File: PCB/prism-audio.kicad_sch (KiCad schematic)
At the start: 8 parts, among them Q1 PMBT3904_215, U1 ADAU1761BCPZ

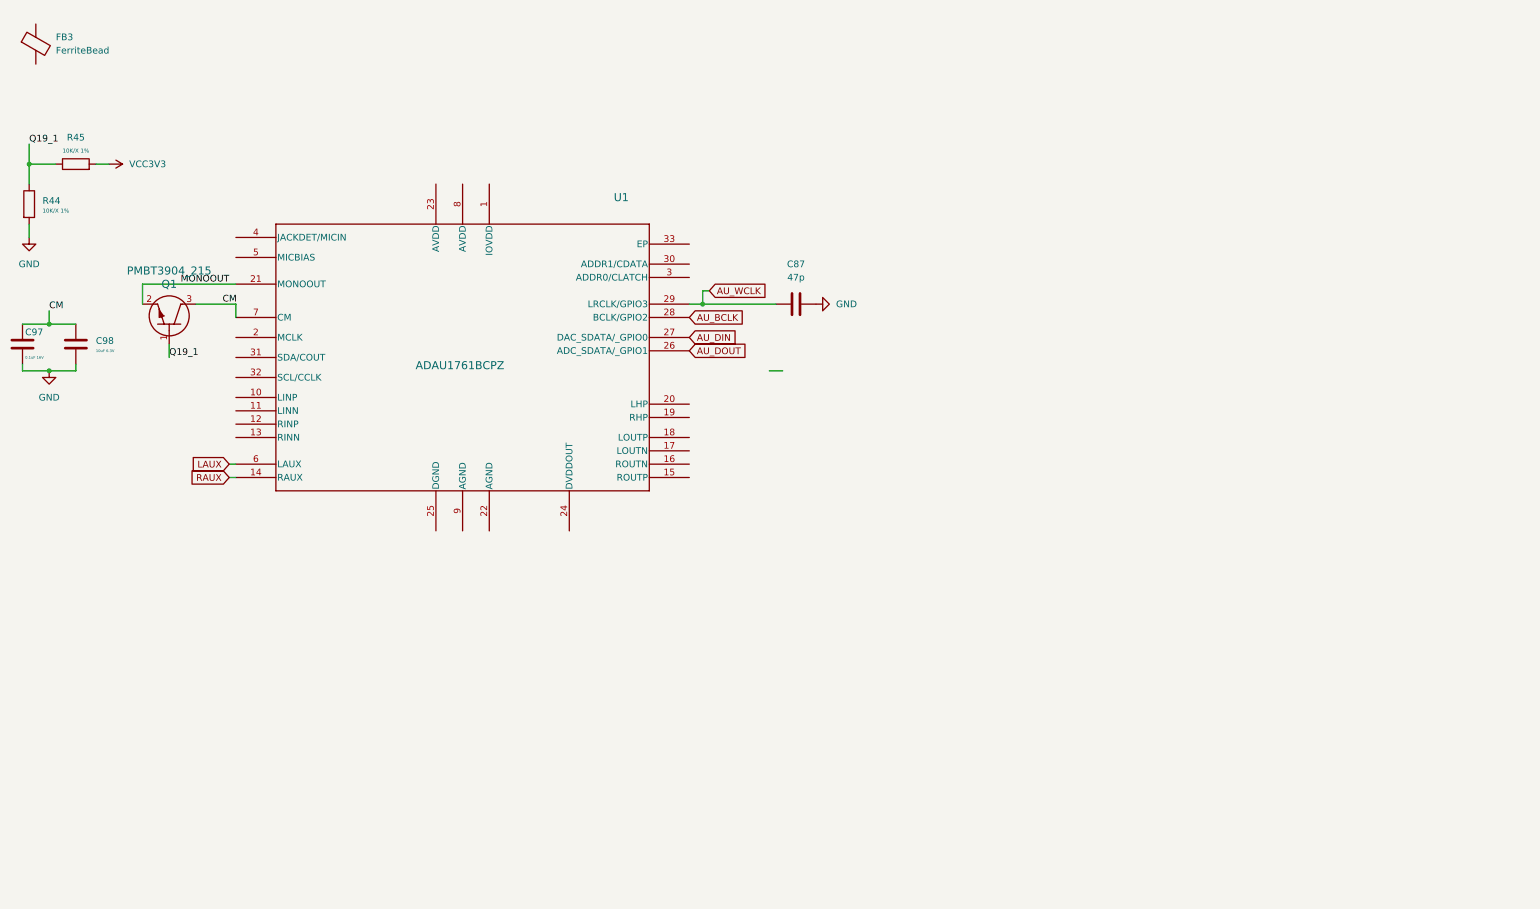
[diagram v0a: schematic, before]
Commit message: Added headphoen audio
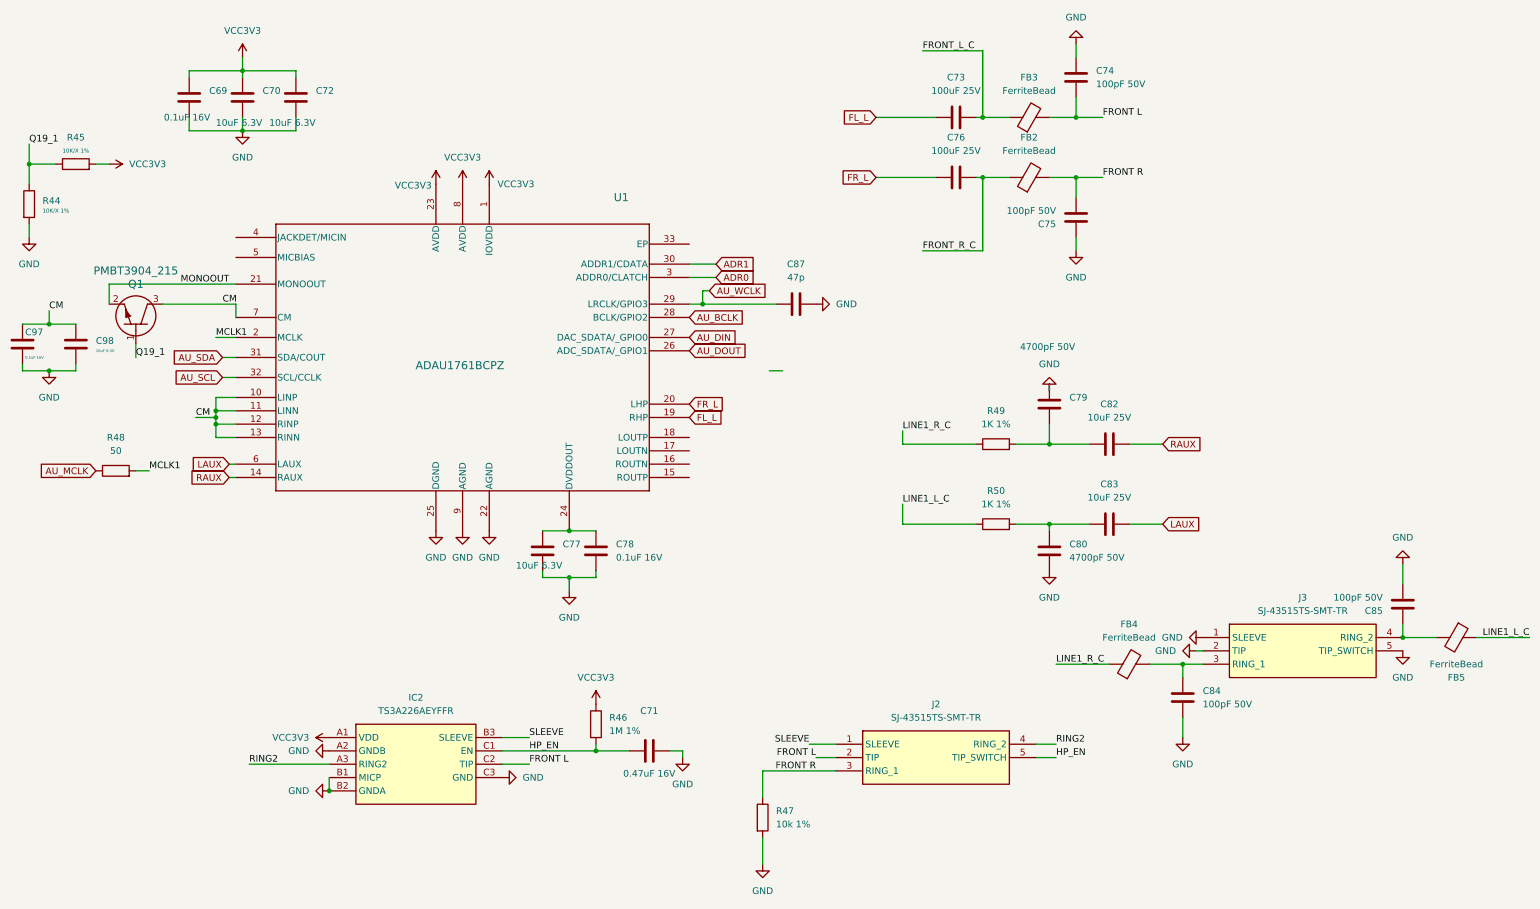
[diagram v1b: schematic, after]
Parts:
- added C69, C78: 0.1uF 16V, symbol Device:C
- added C70, C72, C77: 10uF 6.3V, symbol Device:C
- added C71: 0.47uF 16V, symbol Device:C
- added C73, C76: 100uF 25V, symbol Device:C
- added C74, C75, C84, C85: 100pF 50V, symbol Device:C
- added C79, C80: 4700pF 50V, symbol Device:C
- added C82, C83: 10uF 25V, symbol Device:C
- added FB2, FB4, FB5: FerriteBead, Inductor_SMD:L_0805_2012Metric, symbol Device:FerriteBead
- added IC2: TS3A226AEYFFR, BGA9C40P3X3_126X136X62, symbol TS3A226AEYFFR:TS3A226AEYFFR
- added J2, J3: SJ-43515TS-SMT-TR, SJ43515TSSMTTR, symbol SJ-43515TS-SMT-TR:SJ-43515TS-SMT-TR
- added R46: 1M 1%, symbol Device:R
- added R47: 10k 1%, symbol Device:R
- added R48: 50, symbol Device:R
- added R49, R50: 1K 1%, Resistor_SMD:R_0603_1608Metric, symbol Device:R
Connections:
- net CM: now also U1.10 (LINP), U1.11 (LINN), U1.12 (RINP), U1.13 (RINN)
- net GND: now also U1.22 (AGND), U1.25 (DGND), U1.9 (AGND), C69.2, C70.2, C71.2, C72.2, C74.1, C75.1, C77.2, C78.2, C79.1, C80.2, C84.2, C85.2, IC2.A2 (GNDB), IC2.B1 (MICP), IC2.B2 (GNDA), IC2.C3 (GND), J3.1 (SLEEVE), J3.2 (TIP), J3.5 (TIP_SWITCH), R47.2
- net LAUX: now also C83.2
- net RAUX: now also C82.2
- net VCC3V3: now also U1.1 (IOVDD), U1.23 (AVDD), U1.8 (AVDD), C69.1, C70.1, C72.1, IC2.A1 (VDD), R46.1
- net FL_L: now reaches U1.19 (RHP)
- net FL_L: now also C73.1
- net MCLK1: now reaches U1.2 (MCLK)
- net MCLK1: now also R48.2
- net FR_L: now reaches U1.20 (LHP)
- net FR_L: now also C76.1
- net at U1.24 (DVDDOUT): now also C77.1, C78.1
- net ADR0: now reaches U1.3 (ADDR0/CLATCH)
- net ADR1: now reaches U1.30 (ADDR1/CDATA)
- net AU_SDA: now reaches U1.31 (SDA/COUT)
- net AU_SCL: now reaches U1.32 (SCL/CCLK)
- net FRONT_L_C: now reaches FB3.1
- net FRONT_L_C: now also C73.2
- net FRONT L: now reaches FB3.2
- net FRONT L: now also C74.2, IC2.C2 (TIP), J2.2 (TIP)
- new net: C85.1, FB5.2, J3.4 (RING_2)
- new net: C79.2, C82.1, R49.2
- new net: C84.1, FB4.2, J3.3 (RING_1)
- new net: C80.1, C83.1, R50.2
- new net AU_MCLK: R48.1
- new net FRONT R: C75.2, FB2.2, J2.3 (RING_1), R47.1
- new net FRONT_R_C: C76.2, FB2.1
- new net HP_EN: C71.1, IC2.C1 (EN), J2.5 (TIP_SWITCH), R46.2
- new net LINE1_L_C: FB5.1, R50.1
- new net LINE1_R_C: FB4.1, R49.1
- new net RING2: IC2.A3 (RING2), J2.4 (RING_2)
- new net SLEEVE: IC2.B3 (SLEEVE), J2.1 (SLEEVE)
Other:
- moved on the sheet: FB3, Q1

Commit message: merge commit
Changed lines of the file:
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@@
 	(wire
 		(pts
-			(xy 212.09 135.89) (xy 222.25 135.89)
+			(xy 93.98 40.64) (xy 93.98 44.45)
 		)
 		(stroke
@@
 	(wire
 		(pts
-			(xy 238.76 133.35) (xy 240.03 133.35)
+			(xy 212.09 135.89) (xy 222.25 135.89)
 		)
 		(stroke
@@
 	(wire
 		(pts
-			(xy 142.24 62.23) (xy 147.32 62.23)
+			(xy 238.76 133.35) (xy 240.03 133.35)
 		)
 		(stroke
@@
 	(wire
 		(pts
-			(xy 55.88 85.09) (xy 52.07 85.09)
+			(xy 142.24 62.23) (xy 147.32 62.23)
 		)
 		(stroke
@@
 	(wire
 		(pts
-			(xy 156.21 156.21) (xy 156.21 161.29)
+			(xy 55.88 85.09) (xy 52.07 85.09)
 		)
 		(stroke
@@
 	(wire
 		(pts
-			(xy 157.48 80.01) (xy 160.02 80.01)
+			(xy 156.21 156.21) (xy 156.21 161.29)
 		)
 		(stroke
@@
 	(wire
 		(pts
+			(xy 104.14 40.64) (xy 104.14 44.45)
+		)
+		(stroke
+			(width 0)
+			(type default)
+		)
+	)
+	(wire
+		(pts
 			(xy 55.88 90.17) (xy 52.07 90.17)
 		)
@@
 	(wire
 		(pts
+			(xy 99.06 40.64) (xy 99.06 44.45)
+		)
+		(stroke
+			(width 0)
+			(type default)
+		)
+	)
+	(wire
+		(pts
 			(xy 182.88 93.98) (xy 196.85 93.98)
 		)
@@
 	(symbol
 		(lib_id "power:VCC")
-		(at 93.98 44.45 0)
+		(at 93.98 40.64 0)
 		(unit 1)
 		(exclude_from_sim no)
@@
 		(dnp no)
 		(property "Reference" "#PWR098"
-			(at 93.98 48.26 0)
+			(at 93.98 44.45 0)
 			(effects
 				(font
@@
 		)
 		(property "Value" "VCC3V3"
-			(at 89.662 44.704 0)
+			(at 89.662 40.894 0)
 			(effects
 				(font
@@
 		)
 		(property "Footprint" ""
-			(at 93.98 44.45 0)
+			(at 93.98 40.64 0)
 			(effects
 				(font
@@
 		)
 		(property "Datasheet" ""
-			(at 93.98 44.45 0)
+			(at 93.98 40.64 0)
 			(effects
 				(font
@@
 		)
 		(property "Description" "Power symbol creates a global label with name \"VCC\""
-			(at 93.98 44.45 0)
+			(at 93.98 40.64 0)
 			(effects
 				(font
@@
 	(symbol
 		(lib_id "power:VCC")
-		(at 104.14 44.45 0)
+		(at 104.14 40.64 0)
 		(unit 1)
 		(exclude_from_sim no)
@@
 		(dnp no)
 		(property "Reference" "#PWR0100"
-			(at 104.14 48.26 0)
+			(at 104.14 44.45 0)
 			(effects
 				(font
@@
 		)
 		(property "Value" "VCC3V3"
-			(at 109.22 44.45 0)
+			(at 109.22 40.64 0)
 			(effects
 				(font
@@
 		)
 		(property "Footprint" ""
-			(at 104.14 44.45 0)
+			(at 104.14 40.64 0)
 			(effects
 				(font
@@
 		)
 		(property "Datasheet" ""
-			(at 104.14 44.45 0)
+			(at 104.14 40.64 0)
 			(effects
 				(font
@@
 		)
 		(property "Description" "Power symbol creates a global label with name \"VCC\""
-			(at 104.14 44.45 0)
+			(at 104.14 40.64 0)
 			(effects
 				(font
@@
 	(symbol
 		(lib_id "power:VCC")
-		(at 99.06 44.45 0)
+		(at 99.06 40.64 0)
 		(unit 1)
 		(exclude_from_sim no)
@@
 		(fields_autoplaced yes)
 		(property "Reference" "#PWR099"
-			(at 99.06 48.26 0)
+			(at 99.06 44.45 0)
 			(effects
 				(font
@@
 		)
 		(property "Value" "VCC3V3"
-			(at 99.06 39.37 0)
+			(at 99.06 35.56 0)
 			(effects
 				(font
@@
 		)
 		(property "Footprint" ""
-			(at 99.06 44.45 0)
+			(at 99.06 40.64 0)
 			(effects
 				(font
@@
 		)
 		(property "Datasheet" ""
-			(at 99.06 44.45 0)
+			(at 99.06 40.64 0)
 			(effects
 				(font
@@
 		)
 		(property "Description" "Power symbol creates a global label with name \"VCC\""
-			(at 99.06 44.45 0)
+			(at 99.06 40.64 0)
 			(effects
 				(font
